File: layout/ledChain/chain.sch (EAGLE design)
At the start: 29 parts, among them IC2 FT232RL, P1 FSM4JSMA-SMD, T1 BC848, T2 BC848

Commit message: not quite their
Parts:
- removed IC1: (no value), sid:LM1117IMP
- removed P1: FSM4JSMA-SMD, switch-misc:FSM4JSMA-SMD
- removed R19: 10k, rcl-2:R-EU_R0603
- removed U$40: USB-B, sid:USB-B
- added C8: 100n, rcl:C-EUC0603
- added IC3: ATTINY10, adafruit:ATTINY10
- added S1: DTSM-3, switch-tact:DTSM-3
- added U1: SPX3819M5-L-3-3, ESP8266-2:SPX3819M5-L-3-3
- C1, C6: value 100u -> 68u 6.3V Tantal Poly; device cap-master:CP-7343-TE-D -> rcl-2:C-EUC0805
- U$3: value ATTINY45 -> USB-MALE-SMT; device SparkFun:ATTINY45 -> sid:USB-MALE-SMT
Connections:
- removed net N$12: C2.1, IC2.3V3OUT
- removed net N$2: R19.1, U$2.CH_PD
- new net N$15: C2.1, IC2.3V3OUT, IC2.VCCIO
- new net N$17: C8.1, U1.ADJ/BYP
- net +3V3: now also C6.1, U$2.CH_PD, U1.VOUT; no longer C6.+, IC1.VOUT, IC1.VOUT_TAB, IC2.VCCIO, R19.2
- net +5V: now also C1.1, IC3.VCC, U$3.VBUS, U1.EN, U1.VIN; no longer C1.+, IC1.VIN, U$3.VCC, U$40.VBUS
- net GND: now also C1.2, C6.2, C8.2, IC3.GND, S1.2, U$3.S1, U$3.S2, U1.GND; no longer C1.-, C6.-, IC1.GND, P1.S, P1.S@1, U$40.GND, U$40.P$1, U$40.P$2
- net GPIO0: now also S1.1; no longer P1.P, P1.P@1
- net N$10: now also IC3.PB0, SV2.2; no longer R5.1, U$3.PB2(SCK/ADC1)
- net N$11: now also IC3./RST, R2.1; no longer SV2.2, U$3.PB1(MISO)
- net N$13: now also IC3.PB1; no longer U$3.PB3(ADC3)
- net N$14: now also R5.1; no longer R5.2
- net N$3: now also U$3.D+; no longer U$40.D+
- net N$4: now also U$3.D-; no longer U$40.D-
- net N$6: now also IC3.PB2, R5.2; no longer R2.1, U$3.PB5(NRES)
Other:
- note added: "WS28XX"
- moved on the sheet: C5, C7, R1, R2, R5, U$1

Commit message: before ws281x converter
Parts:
- added IC4: ATTINY85-20S, avr:ATTINY85-20S
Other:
- note added: "74HCT2G14 hat aber farnell nicht"
- note added: "QUARZ"
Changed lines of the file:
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@@
 <part name="U$3" library="sid" deviceset="USB-MALE-SMT" device=""/>
 <part name="S1" library="switch-tact" deviceset="DTSM-3" device=""/>
+<part name="IC4" library="avr" deviceset="ATTINY85" device="S" technology="-20"/>
 </parts>
 <sheets>
@@
 <text x="228.6" y="139.7" size="1.778" layer="94">data</text>
 <text x="154.94" y="109.22" size="1.778" layer="94">WS28XX</text>
+<text x="127" y="-5.08" size="1.778" layer="94">QUARZ</text>
+<text x="160.02" y="-5.08" size="1.778" layer="94">74HCT2G14 hat aber farnell nicht</text>
 </plain>
 <instances>
@@
 <instance part="U$3" gate="G$1" x="27.94" y="35.56"/>
 <instance part="S1" gate="G$1" x="137.16" y="149.86" rot="R180"/>
+<instance part="IC4" gate="G$1" x="81.28" y="0"/>
 </instances>
 <busses>

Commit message: power rails done
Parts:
- removed IC3: ATTINY10, adafruit:ATTINY10
- removed R1, R5: 470, rcl-2:R-EU_R0603
- removed R2: 10k, rcl-2:R-EU_R0603
- removed SJ1: (no value), jumper:SJ2W
- added Q1: 25mhz, sid:KC5032A
- U$1: value BSS138 -> 74HCT2G14GWQ100; device m-pad-1.5:BSS138 -> sid:74HCT2G14
- renumbered SV2 to SV1
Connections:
- removed net N$10: IC3.PB0, SV1.2
- removed net N$11: IC3./RST, R2.1
- removed net N$13: IC3.PB1, SJ1.3
- removed net N$14: R1.1, R5.1, SJ1.1, U$1.D
- removed net N$6: IC3.PB2, R5.2
- removed net N$9: SJ1.2, SV1.3
- new net N$2: IC4.(XTAL1/CLKI/OC1B/ADC3/PCINT3)PB3, Q1.FO
- new net WSCLK: IC4.(MOSI/DI/SDA/AIN0/OC0A/OC1A/AREF/PCINT0)PB0, SV1.3, U$1.1Y
- new net WSDATA: IC4.(MISO/DO/AIN1/OC0B/OC1A/PCINT1)PB1, SV1.2, U$1.2Y
- net +5V: now also IC4.VCC, Q1.VCC, SV1.4, U$1.VCC; no longer IC3.VCC, R1.2, R2.2, SV1.1
- net GND: now also IC4.GND, Q1.GND, SV1.1, U$1.GND; no longer IC3.GND, SV1.4, U$1.S
- net GPIO15: now also IC4.(XTAL2/CLKO/OC1B/ADC2/PCINT4)PB4
- net GPIO2: now also IC4.(SCK/USCK/SCL/ADC1/T0/INT0/PCINT2)PB2, U$1.1A, U$1.2A; no longer U$1.G
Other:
- note removed: "74HCT2G14 hat aber farnell nicht"
- note removed: "QUARZ"
- note removed: "clk"
- note removed: "data"
- moved on the sheet: IC4

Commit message: challenge accepted and passed
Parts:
- added C10: 100n, rcl:C-EUC0603
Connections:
- net +3V3: now also C10.1, IC2.VCCIO
- net GND: now also C10.2
- net N$15: no longer IC2.VCCIO
- net WSCLK: now also U$1.2Y; no longer U$1.1Y
- net WSDATA: now also U$1.1Y; no longer U$1.2Y
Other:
- note added: "alternative:"
- moved on the sheet: C2, IC2, R3, R4, T1, T2

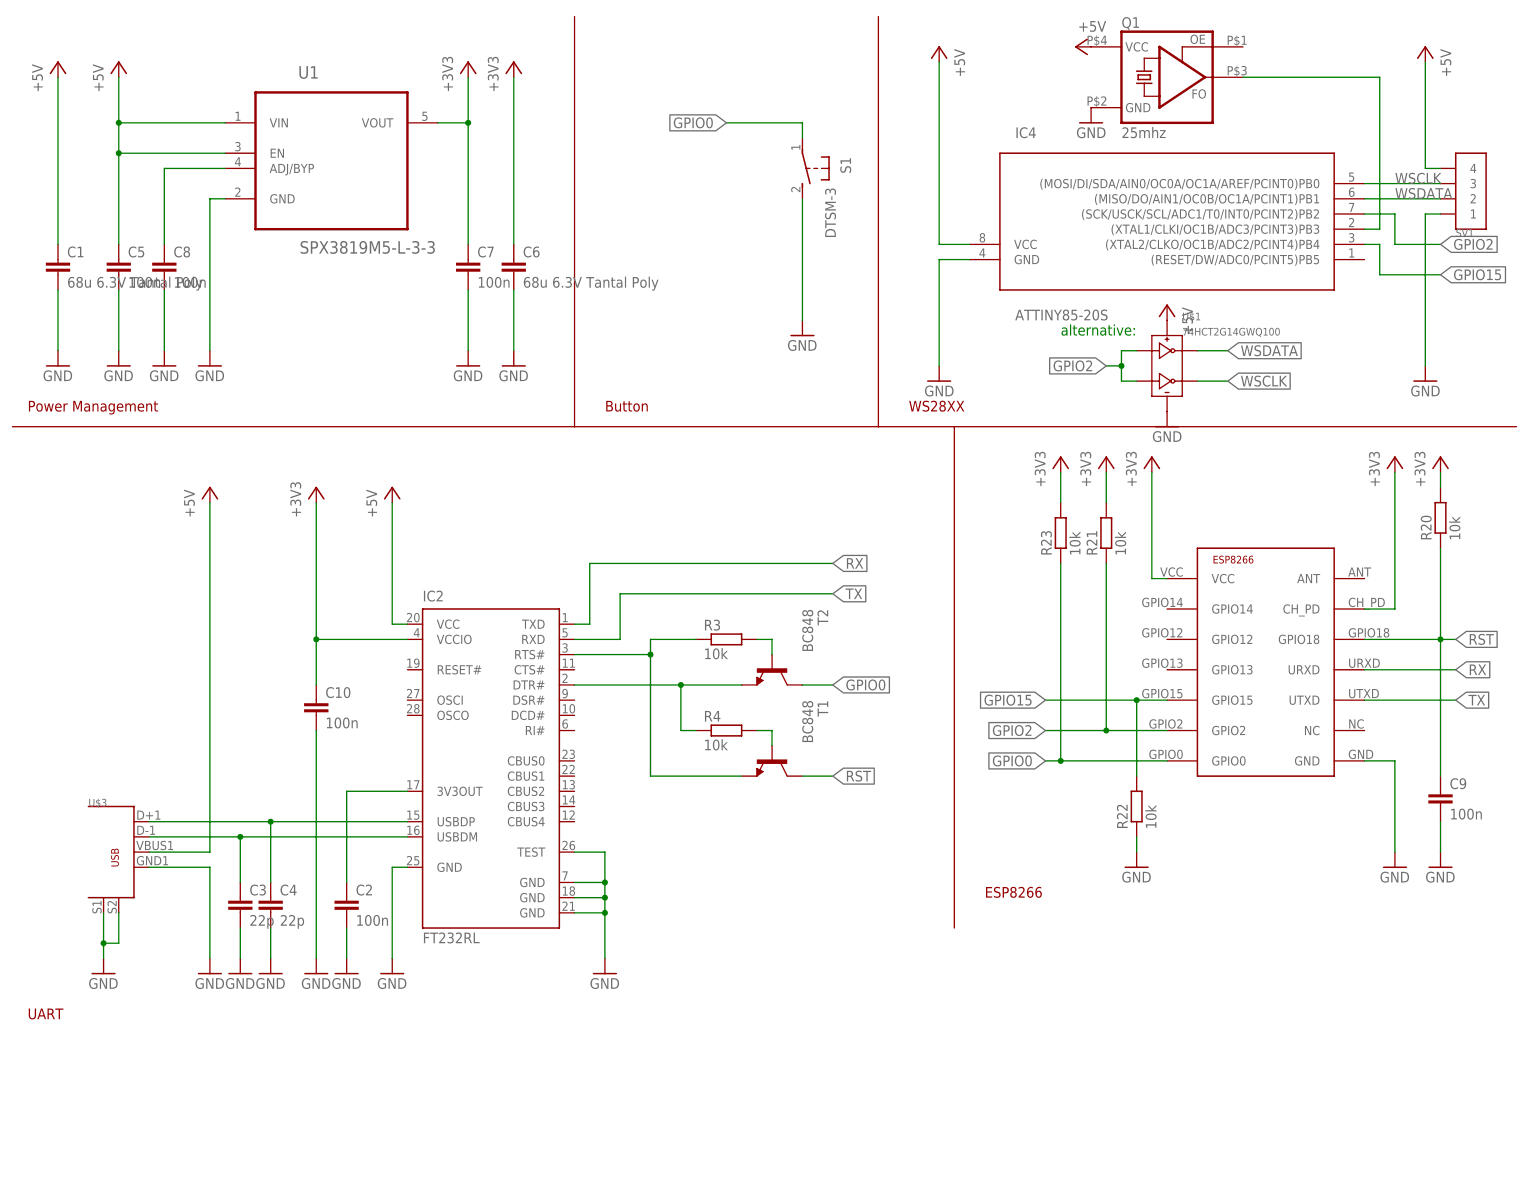
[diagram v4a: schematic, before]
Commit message: Schaltplan für ledChain hinzugefügt. Bauteilbezeichnungen sortiert.
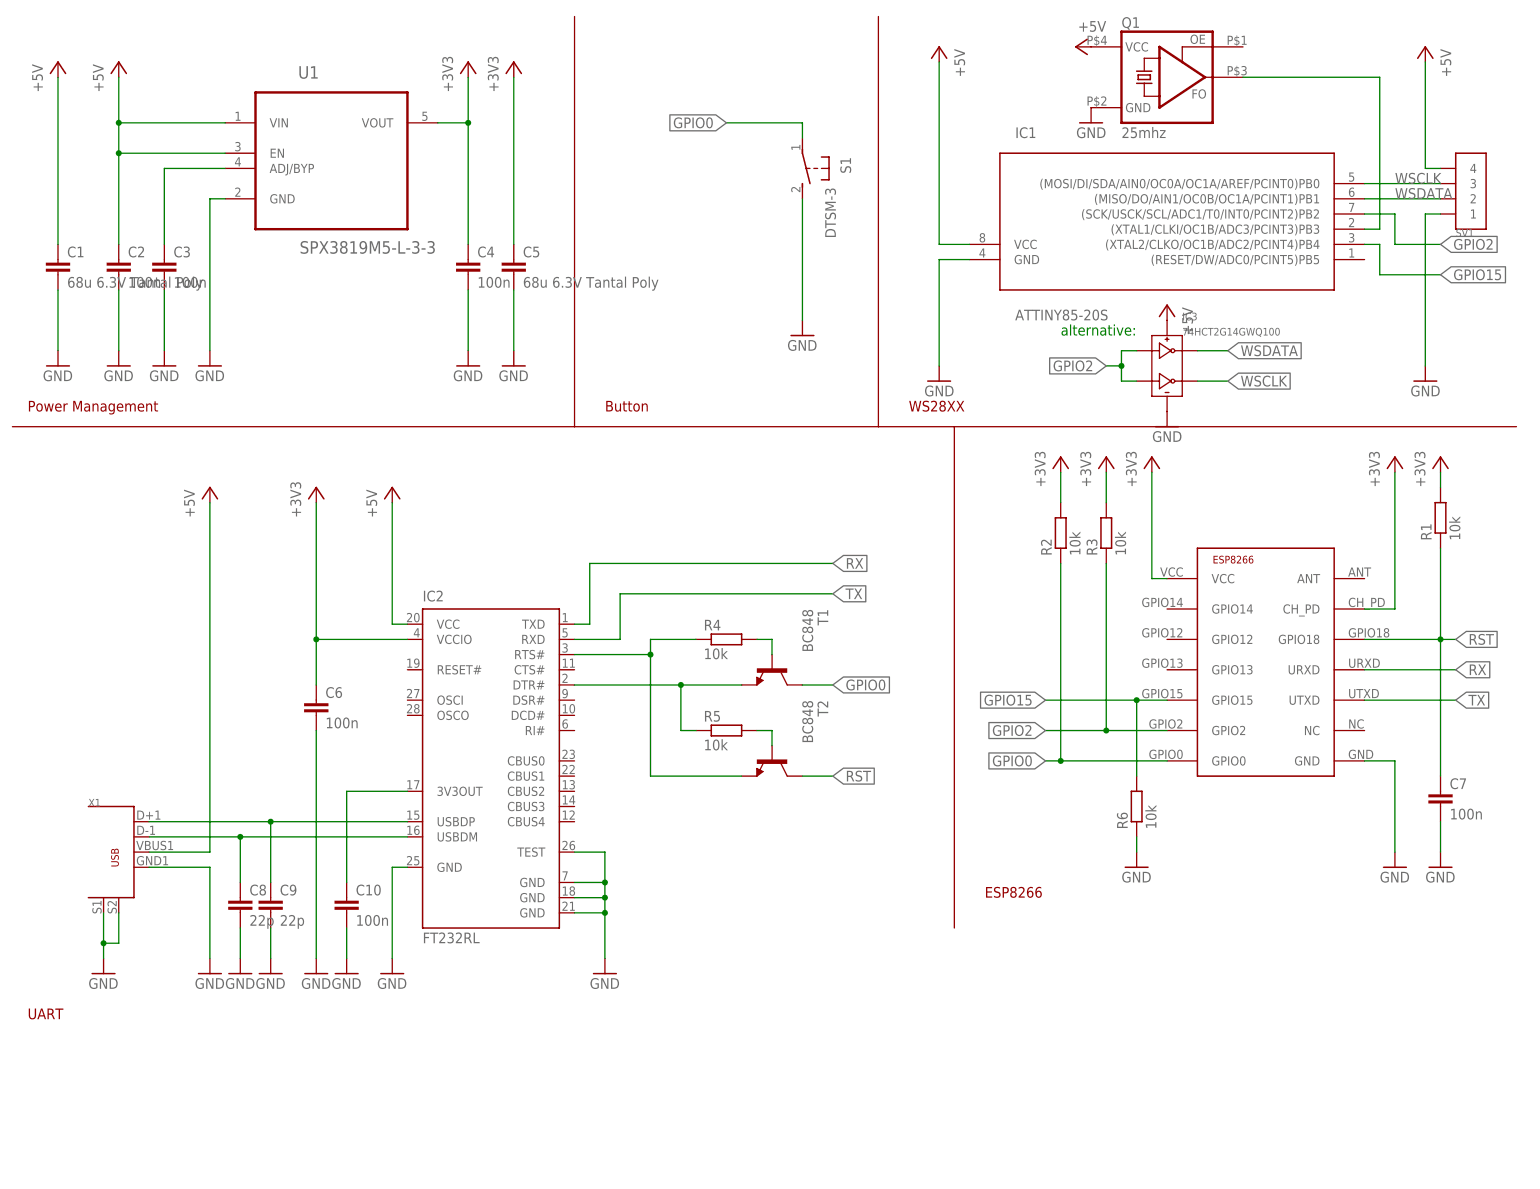
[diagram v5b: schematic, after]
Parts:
- removed R21: 10k, rcl-2:R-EU_R0603
- added R5: 10k, rcl-2:R-EU_R0603
- C3, C4: value 22p -> 100n
- C5: value 100n -> 68u 6.3V Tantal Poly; device rcl:C-EUC0603 -> rcl-2:C-EUC0805
- C6: value 68u 6.3V Tantal Poly -> 100n; device rcl-2:C-EUC0805 -> rcl:C-EUC0603
- C8, C9: value 100n -> 22p
- renumbered IC4 to IC1, R20 to R1, R22 to R6, R23 to R2, U$1 to IC3, U$3 to X1
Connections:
- removed net N$7 (its old number): R3.2, T2.B
- new net N$8: R5.2, T2.B
- net +3V3: now also C4.1, C5.1, R3.2; no longer C10.1, C7.1, R21.2
- net +5V: now also C2.1; no longer C5.1
- net GPIO0: now also T1.C; no longer T2.C
- net GPIO2: now also R3.1; no longer R21.1
- net N$1: now also R4.1, T2.E; no longer R3.1, T1.E
- net N$15: now also C10.1; no longer C2.1
- net N$17: now also C3.1; no longer C8.1
- net N$3: now also C9.1; no longer C4.1
- net N$4: now also C8.1; no longer C3.1
- net N$5: now also R5.1, T1.E; no longer R4.1, T2.E
- net RST: now also C7.1, T2.C; no longer C9.1, T1.C
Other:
- moved on the sheet: C10, C2, C3, C4, C5, C6, C7, C8, C9, R3, R4, T1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
